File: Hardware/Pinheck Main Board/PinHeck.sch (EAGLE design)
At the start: 365 parts, among them IC2 PIC32MX795F512L-80I/PT, IC3 CD74HCT244E, IC4 CD74HCT244E, IC5 ULN2803A, P1 TC33X-2-103E, U1 P8X32A-Q44, U10 74HCT2G04GV,125, U11 CD74HC165M96, U12 CD74HC165M96, U13 CAT24M01LI-G, U14 MC74HC08ADR2G, U15 MC74HC08ADR2G, U16 MC74HC08ADR2G, U17 MC74HC08ADR2G, U18 MC74HC08ADR2G, U19 MC74HC08ADR2G, U2 DS1340Z-33+, U20 TIP107, U21 TIP107, U22 TIP107, U23 TIP107, U24 TIP107, U25 TIP107, U26 TIP107, U27 TIP107, U28 TIP102, U29 TIP102, U3 CD74HC595M96, U30 TIP102, U31 TIP102, U32 TIP102, U33 TIP102, U34 TIP102, U35 TIP102, U36 WS2801, U37 TIP107, U38 WS2801, U39 NCP1117DT33G, U4 CAT24M01LI-G, U5 CD74HC595M96, U52 CD74HC123M96, X1 FQ7050B-8.000, X2 9C-6.500MAAJ-T, X3 ABS25-32.768KHz-1-T

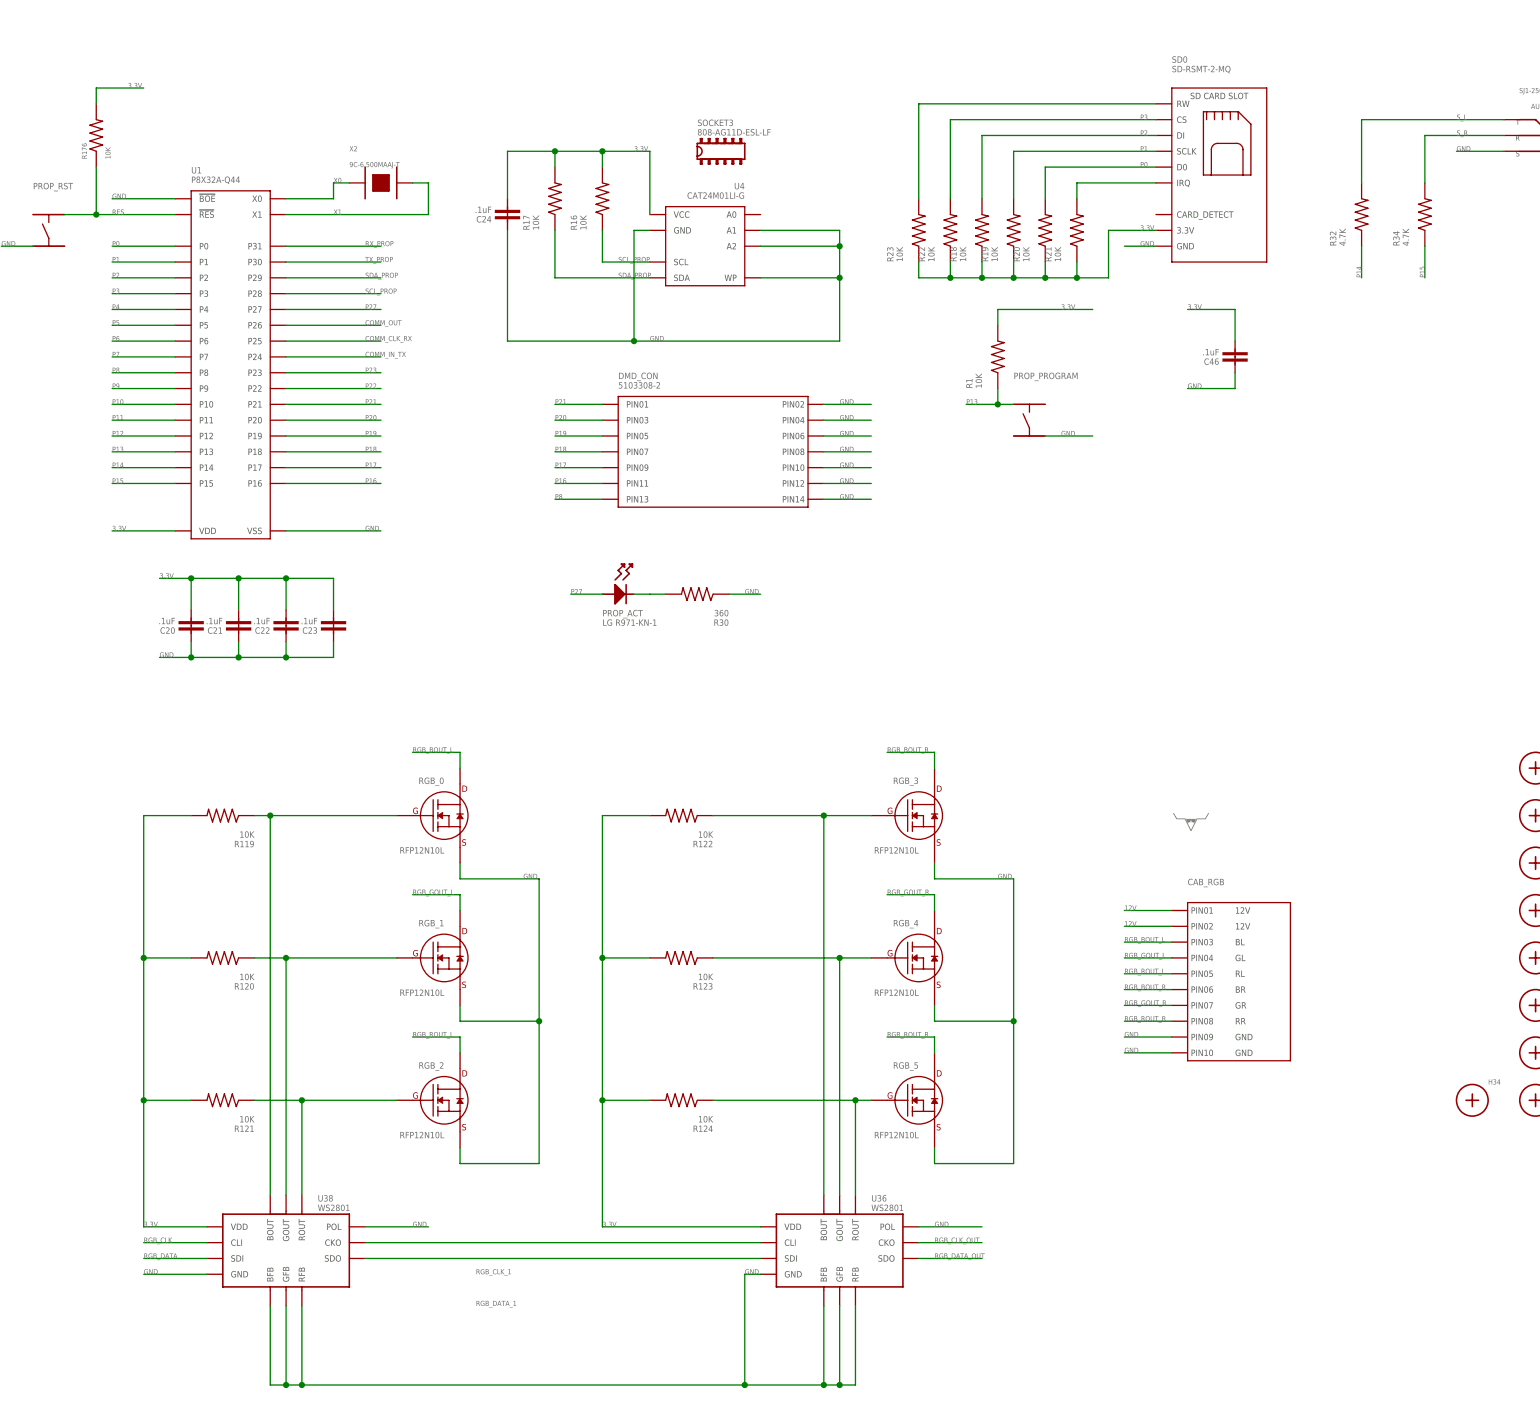
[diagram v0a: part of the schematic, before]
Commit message: Prop routed. Pic32 started.
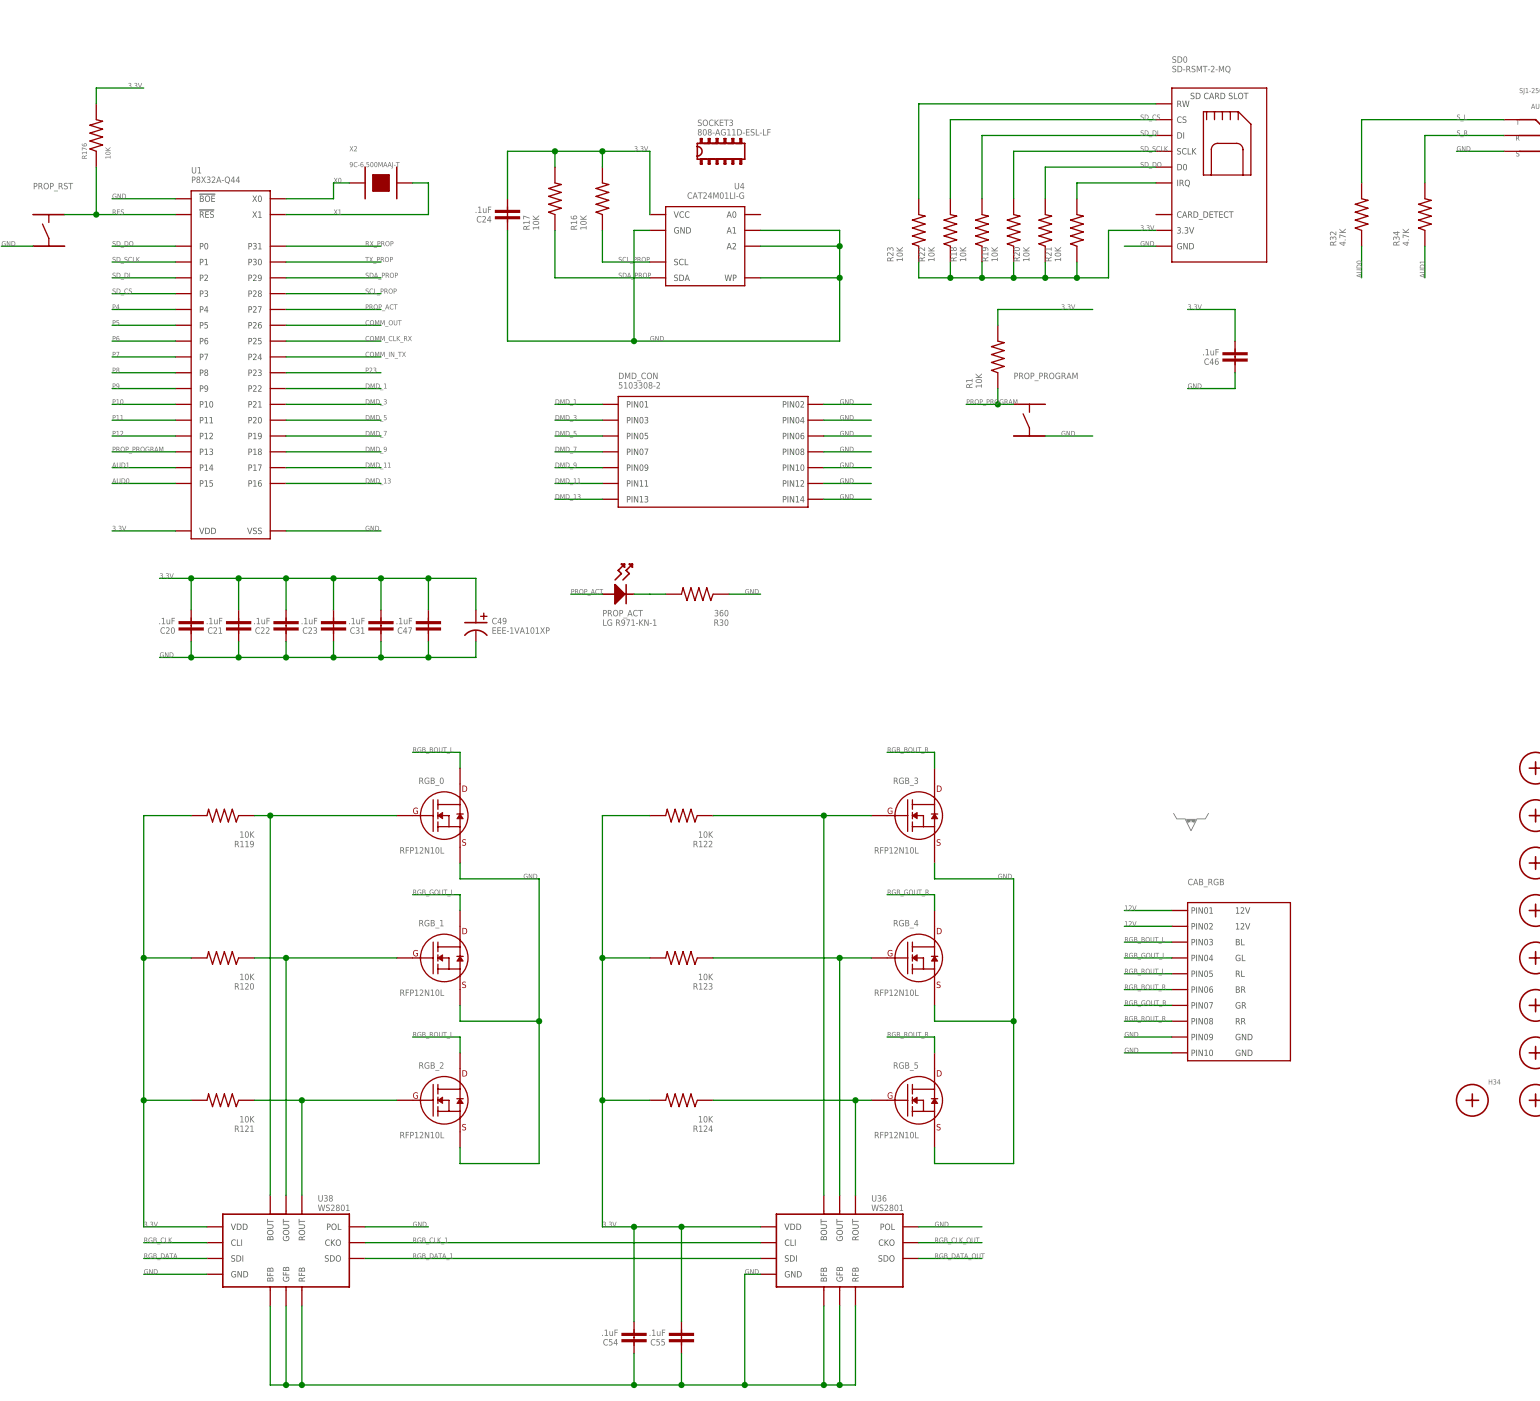
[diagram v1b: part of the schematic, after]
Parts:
- added C31, C47, C54, C55: .1uF, PP_Passives:CAPACITOR_NON_POLAR_0805
- added C49: EEE-1VA101XP, PP_Passives:CAPACITOR_POLARIZED_6.3MM_SMD
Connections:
- net N$24 renamed SD_IQ
- net P0 renamed SD_DO
- net P1 renamed SD_SCLK
- net P13 renamed PROP_PROGRAM
- net P2 renamed SD_DI
- net P27 renamed PROP_ACT
- net P3 renamed SD_CS
- removed net P14: R32.1, U1.P14
- removed net P15: R34.1, U1.P15
- removed net P16: DMD_CON.PIN11, U1.P16
- removed net P17: DMD_CON.PIN9, U1.P17
- removed net P18: DMD_CON.PIN7, U1.P18
- removed net P19: DMD_CON.PIN5, U1.P19
- removed net P20: DMD_CON.PIN3, U1.P20
- removed net P21: DMD_CON.PIN1, U1.P21
- removed net P22: U1.P22
- new net AUD0: R32.1, U1.P15
- new net AUD1: R34.1, U1.P14
- new net DMD_1: DMD_CON.PIN1, U1.P22
- new net DMD_11: DMD_CON.PIN11, U1.P17
- new net DMD_13: DMD_CON.PIN13, U1.P16
- new net DMD_3: DMD_CON.PIN3, U1.P21
- new net DMD_5: DMD_CON.PIN5, U1.P20
- new net DMD_7: DMD_CON.PIN7, U1.P19
- new net DMD_9: DMD_CON.PIN9, U1.P18
- net 3.3V: now also C31.2, C47.2, C49.POS, C54.2, C55.2
- net GND: now also C31.1, C47.1, C49.NEG, C54.1, C55.1
- net P8: no longer DMD_CON.PIN13

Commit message: Home stretch!
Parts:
- removed D8: NSQA6V8AW5T2G, Discrete:NSQA6V8
- MOD_CON: device PP_Connectors:CON_01X05_2.54MM_PIN_HEADER -> PP_Connectors:CON_01X06_2.54MM_PIN_HEADER
- renumbered U37 to ST_LI
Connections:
- removed net !AN_BLANK: U10.2Y
- net 12V: now also MOD_CON.6
- net 3.3V: now also MOD_CON.2; no longer MOD_CON.PIN2
- net 5V: now also MOD_CON.3; no longer MOD_CON.PIN3
- net AUX_3: now also R15.1; no longer R5.1
- net AUX_4: now also R10.1; no longer R7.1
- net AUX_5: now also R7.1; no longer R10.1
- net AUX_6: now also R5.1; no longer R15.1
- net GND: now also MOD_CON.1; no longer D8.COM, MOD_CON.PIN1
- net I2C_SCL: now also MOD_CON.5; no longer MOD_CON.PIN5
- net I2C_SDA: now also MOD_CON.4; no longer MOD_CON.PIN4
- net N$31: no longer D8.D3
- net N$33: no longer D8.D4
- net P32_MCLR: no longer D8.D2
- net WATCHDOG: no longer U10.2A

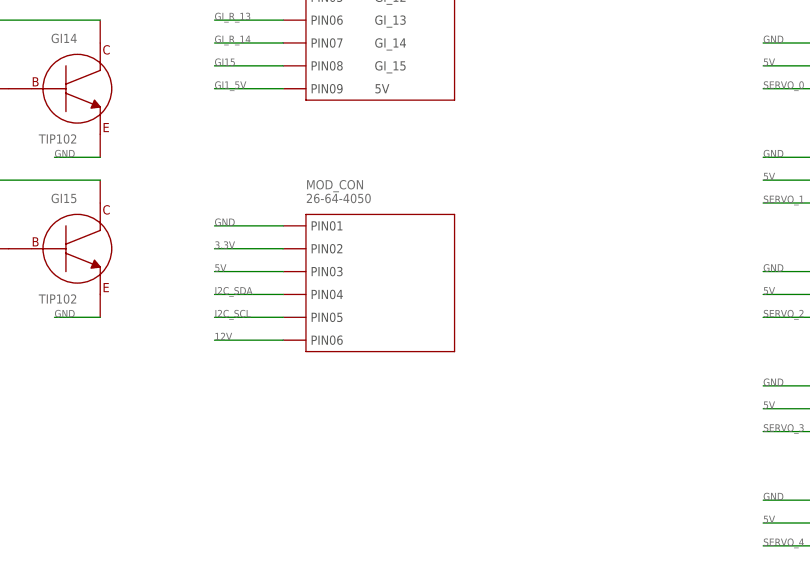
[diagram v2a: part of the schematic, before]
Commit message: MOD CON area done. Starting test header.
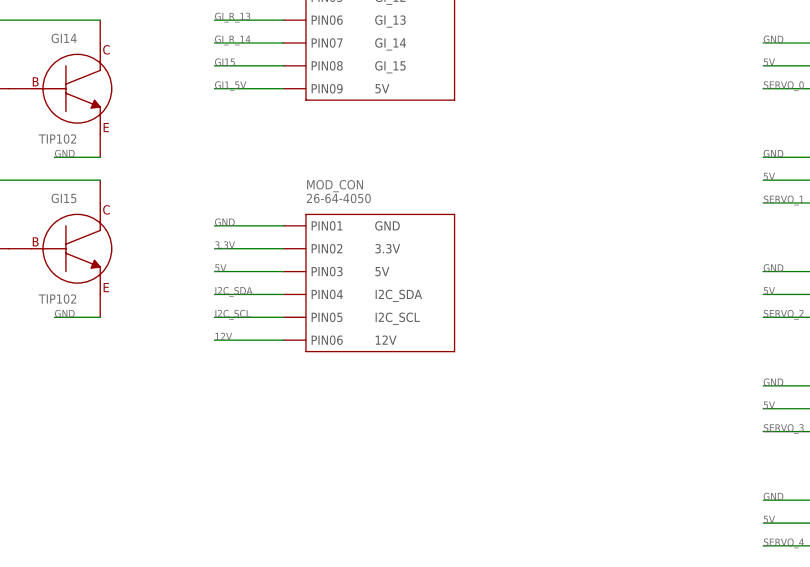
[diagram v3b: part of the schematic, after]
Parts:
- MOD_CON: LABEL01 (none) -> GND; LABEL02 (none) -> 3.3V; LABEL03 (none) -> 5V; LABEL04 (none) -> I2C_SDA; LABEL05 (none) -> I2C_SCL; LABEL06 (none) -> 12V
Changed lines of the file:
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@@
 <part name="SERVO_3" library="PP_Connectors" deviceset="CON_01X03" device="_640454-3" value="640454-3"/>
 <part name="SERVO_4" library="PP_Connectors" deviceset="CON_01X03" device="_640454-3" value="640454-3"/>
-<part name="MOD_CON" library="PP_Connectors" deviceset="CON_01X06" device="_2.54MM_PIN_HEADER" value="26-64-4050"/>
+<part name="MOD_CON" library="PP_Connectors" deviceset="CON_01X06" device="_2.54MM_PIN_HEADER" value="26-64-4050">
+<attribute name="LABEL01" value="GND"/>
+<attribute name="LABEL02" value="3.3V"/>
+<attribute name="LABEL03" value="5V"/>
+<attribute name="LABEL04" value="I2C_SDA"/>
+<attribute name="LABEL05" value="I2C_SCL"/>
+<attribute name="LABEL06" value="12V"/>
+</part>
 <part name="R2" library="PP_Passives" deviceset="RESISTOR" device="_0805" value="2K"/>
 <part name="R5" library="PP_Passives" deviceset="RESISTOR" device="_0805" value="1K"/>

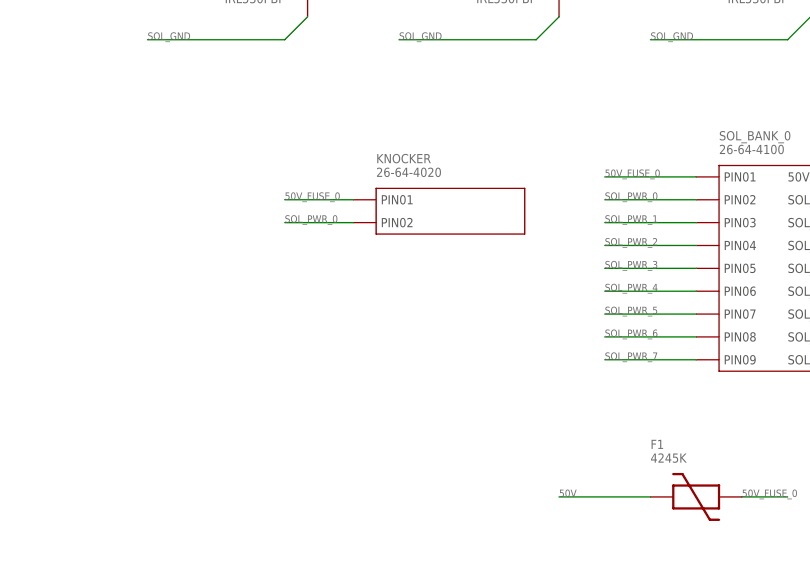
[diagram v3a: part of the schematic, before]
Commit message: Added Shaker connector.
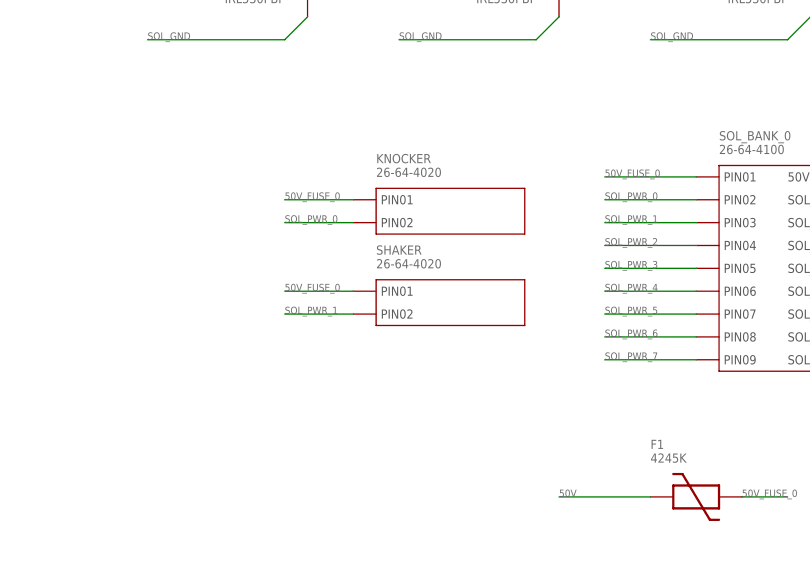
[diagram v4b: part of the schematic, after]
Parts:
- added SHAKER: 26-64-4020, PP_Connectors:CON_01X02_26-64-4020
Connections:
- net 50V_FUSE_0: now also SHAKER.PIN1
- net SOL_PWR_1: now also SHAKER.PIN2
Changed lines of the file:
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@@
 <part name="C54" library="PP_Passives" deviceset="CAPACITOR_NON_POLAR" device="_0805" value=".1uF"/>
 <part name="C55" library="PP_Passives" deviceset="CAPACITOR_NON_POLAR" device="_0805" value=".1uF"/>
+<part name="SHAKER" library="PP_Connectors" deviceset="CON_01X02" device="_26-64-4020" value="26-64-4020"/>
 </parts>
 <sheets>
@@
 <instance part="C54" gate="G$1" x="139.7" y="-162.56" rot="R180"/>
 <instance part="C55" gate="G$1" x="147.32" y="-162.56" rot="R180"/>
+<instance part="SHAKER" gate="G$1" x="581.66" y="71.12"/>
 </instances>
 <busses>
@@
 <pinref part="KNOCKER" gate="G$1" pin="PIN1"/>
 </segment>
+<segment>
+<wire x1="571.5" y1="71.12" x2="579.12" y2="71.12" width="0.1524" layer="91"/>
+<label x="571.5" y="71.12" size="0.8128" layer="95" font="vector"/>
+<pinref part="SHAKER" gate="G$1" pin="PIN1"/>
+</segment>
 </net>
 <net name="SOL_PWR_0" class="0">
@@
 <pinref part="SOL_BANK_0" gate="G$1" pin="PIN3"/>
 </segment>
+<segment>
+<wire x1="579.12" y1="68.58" x2="571.5" y2="68.58" width="0.1524" layer="91"/>
+<label x="571.5" y="68.58" size="0.8128" layer="95" font="vector"/>
+<pinref part="SHAKER" gate="G$1" pin="PIN2"/>
+</segment>
 </net>

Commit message: Added RGB_COM_OUT_1
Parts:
- added RGB_COM_OUT_1: 26-64-4080, PP_Connectors:CON_01X07_26-64-4080(KEYPIN2)
- MOD_CON: device PP_Connectors:CON_01X06_2.54MM_PIN_HEADER -> PP_Connectors:CON_01X08_2.54MM_PIN_HEADER; LABEL07 (none) -> SERVO_3; LABEL08 (none) -> SERVO_4
- OPTO_1, OPTO_2, OPTO_3, OPTO_4, OPTO_5, OPTO_6, OPTO_7: value (none) -> 26-64-4040
- renumbered RGB_COM_OUT to RGB_COM_OUT_0
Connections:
- removed net P4: U1.P4
- removed net P5: U1.P5
- removed net P6: U1.P6
- removed net P7: U1.P7
- new net EXT_RGB_CLK_1: RGB_COM_OUT_1.3, U1.P5
- new net EXT_RGB_DATA_1: RGB_COM_OUT_1.2, U1.P4
- new net PROP_AUX0: RGB_COM_OUT_1.4, U1.P6
- new net PROP_AUX1: RGB_COM_OUT_1.5, U1.P7
- net 12V: now also RGB_COM_OUT_1.6
- net 5V: now also RGB_COM_OUT_1.7
- net GND: now also RGB_COM_OUT_1.1
- net SERVO_3: now also MOD_CON.7
- net SERVO_4: now also MOD_CON.8

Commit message: Added more things to PHAM.
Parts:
- removed RGB_COM_OUT_0: 26-64-4050, PP_Connectors:CON_01X04_26-64-4050(KEYPIN2)
- MOD_CON: device PP_Connectors:CON_01X08_2.54MM_PIN_HEADER -> PP_Connectors:CON_01X20_2.54MM_PIN_HEADER; LABEL06 12V -> GND; LABEL07 SERVO_3 -> 12V; LABEL08 SERVO_4 -> GND; LABEL09 (none) -> SERVO_3; LABEL10 (none) -> SERVO_4; LABEL11 (none) -> GND; LABEL12 (none) -> PROP_AUX2; LABEL13 (none) -> PROP_AUX3; LABEL14 (none) -> PROP_AUX4; LABEL15 (none) -> PROP_AUX5; LABEL16 (none) -> PROP_AUX6; LABEL17 (none) -> PROP_AUX7; LABEL18 (none) -> PROP_AUX8
- renumbered H29 to H2, PROP_PROGRAM to PROP_CONFIG, RGB_COM_OUT_1 to RGB_COM_OUT
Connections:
- net P23 renamed PROP_AUX9
- removed net EXT_RGB_CLK_1: RGB_COM_OUT.3, U1.P5
- removed net EXT_RGB_DATA_1: RGB_COM_OUT.2, U1.P4
- removed net P10: U1.P10
- removed net P11: U1.P11
- removed net P12: U1.P12
- removed net P8: U1.P8
- removed net P9: U1.P9
- new net N$42: MOD_CON.19
- new net N$44: MOD_CON.20
- new net PROP_AUX2: MOD_CON.12, U1.P6
- new net PROP_AUX3: MOD_CON.13, U1.P7
- new net PROP_AUX4: MOD_CON.14, U1.P8
- new net PROP_AUX5: MOD_CON.15, U1.P9
- new net PROP_AUX6: MOD_CON.16, U1.P10
- new net PROP_AUX7: MOD_CON.17, U1.P11
- new net PROP_AUX8: MOD_CON.18, U1.P12
- net 12V: now also MOD_CON.7; no longer MOD_CON.6
- net 5V: no longer RGB_COM_OUT_0.4
- net EXT_RGB_CLK: now also RGB_COM_OUT.5; no longer RGB_COM_OUT_0.3
- net EXT_RGB_DATA: now also RGB_COM_OUT.4; no longer RGB_COM_OUT_0.2
- net GND: now also MOD_CON.11, MOD_CON.6, MOD_CON.8; no longer RGB_COM_OUT_0.1
- net PROP_AUX0: now also RGB_COM_OUT.3, U1.P4; no longer RGB_COM_OUT.4, U1.P6
- net PROP_AUX1: now also RGB_COM_OUT.2, U1.P5; no longer RGB_COM_OUT.5, U1.P7
- net SERVO_3: now also MOD_CON.9; no longer MOD_CON.7
- net SERVO_4: now also MOD_CON.10; no longer MOD_CON.8

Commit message: Adding fuses.
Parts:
- removed P1: TC33X-2-103E, PP_Passives:TC33X-1_TC33X-1
- added C56, C57: .1uF, PP_Passives:CAPACITOR_NON_POLAR_0805
- added F6: 4628, PP_Passives:PTC_FUSE_4628
- added H3, H4: MOUNT_HOLE150MIL, PP_Connectors:MOUNT_HOLE150MIL
- added R147, R148, R149, R150, R151, R152, R153, R154, R155, R156: 100, PP_Passives:RESISTOR_0805
- F1, F2, F3, F4, F5: value 4245K -> 4628; device PP_Passives:PTC_FUSE_4245K -> PP_Passives:PTC_FUSE_4628
- R134: value 20K -> 25K
- U11, U12: value CD74HC165M96 -> 74HC165D-Q100,118
- renumbered MOD_CON to PHABULOUS
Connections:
- removed net N$497: P1.2_WIPER, R134.1
- new net N$17: CABINET.2, R147.1
- new net N$18: CABINET.3, R148.1
- new net N$24: CABINET.4, R149.1
- new net N$27: CABINET.5, R150.1
- new net N$30: CABINET.6, R151.1
- new net N$32: CABINET.7, R152.1
- new net N$35: CABINET.8, R153.1
- new net N$36: CABINET.9, R154.1
- new net N$39: CABINET.10, R155.1
- new net N$46: CABINET.11, R156.1
- new net SERVO_5V: F6.P$2, SERVO_0.PIN2, SERVO_1.PIN2, SERVO_2.PIN2, SERVO_3.PIN2, SERVO_4.PIN2
- net 3.3V: now also C56.1, C57.1
- net 5V: now also F6.P$1; no longer SERVO_0.PIN2, SERVO_1.PIN2, SERVO_2.PIN2, SERVO_3.PIN2, SERVO_4.PIN2
- net BACK: now also R152.2; no longer CABINET.7
- net COIN: now also R150.2; no longer CABINET.5
- net DOOR: now also R153.2; no longer CABINET.8
- net ENTER: now also R151.2; no longer CABINET.6
- net GND: now also C56.2, C57.2
- net L_FLIP: now also R156.2; no longer CABINET.11
- net R_FLIP: now also R155.2; no longer CABINET.10
- net ST_BU: now also R148.2; no longer CABINET.3
- net ST_LI: now also R147.2; no longer CABINET.2
- net TILT: now also R149.2; no longer CABINET.4
- net USER_0: now also R154.2; no longer CABINET.9
- net WATCHDOG_ADJUST: now also R134.1; no longer P1.3_CW
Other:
- moved on the sheet: C6, C8, C9, CABINET, H33, H34, R3
